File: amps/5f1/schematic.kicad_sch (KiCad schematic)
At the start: 26 parts, among them T2 8k:8

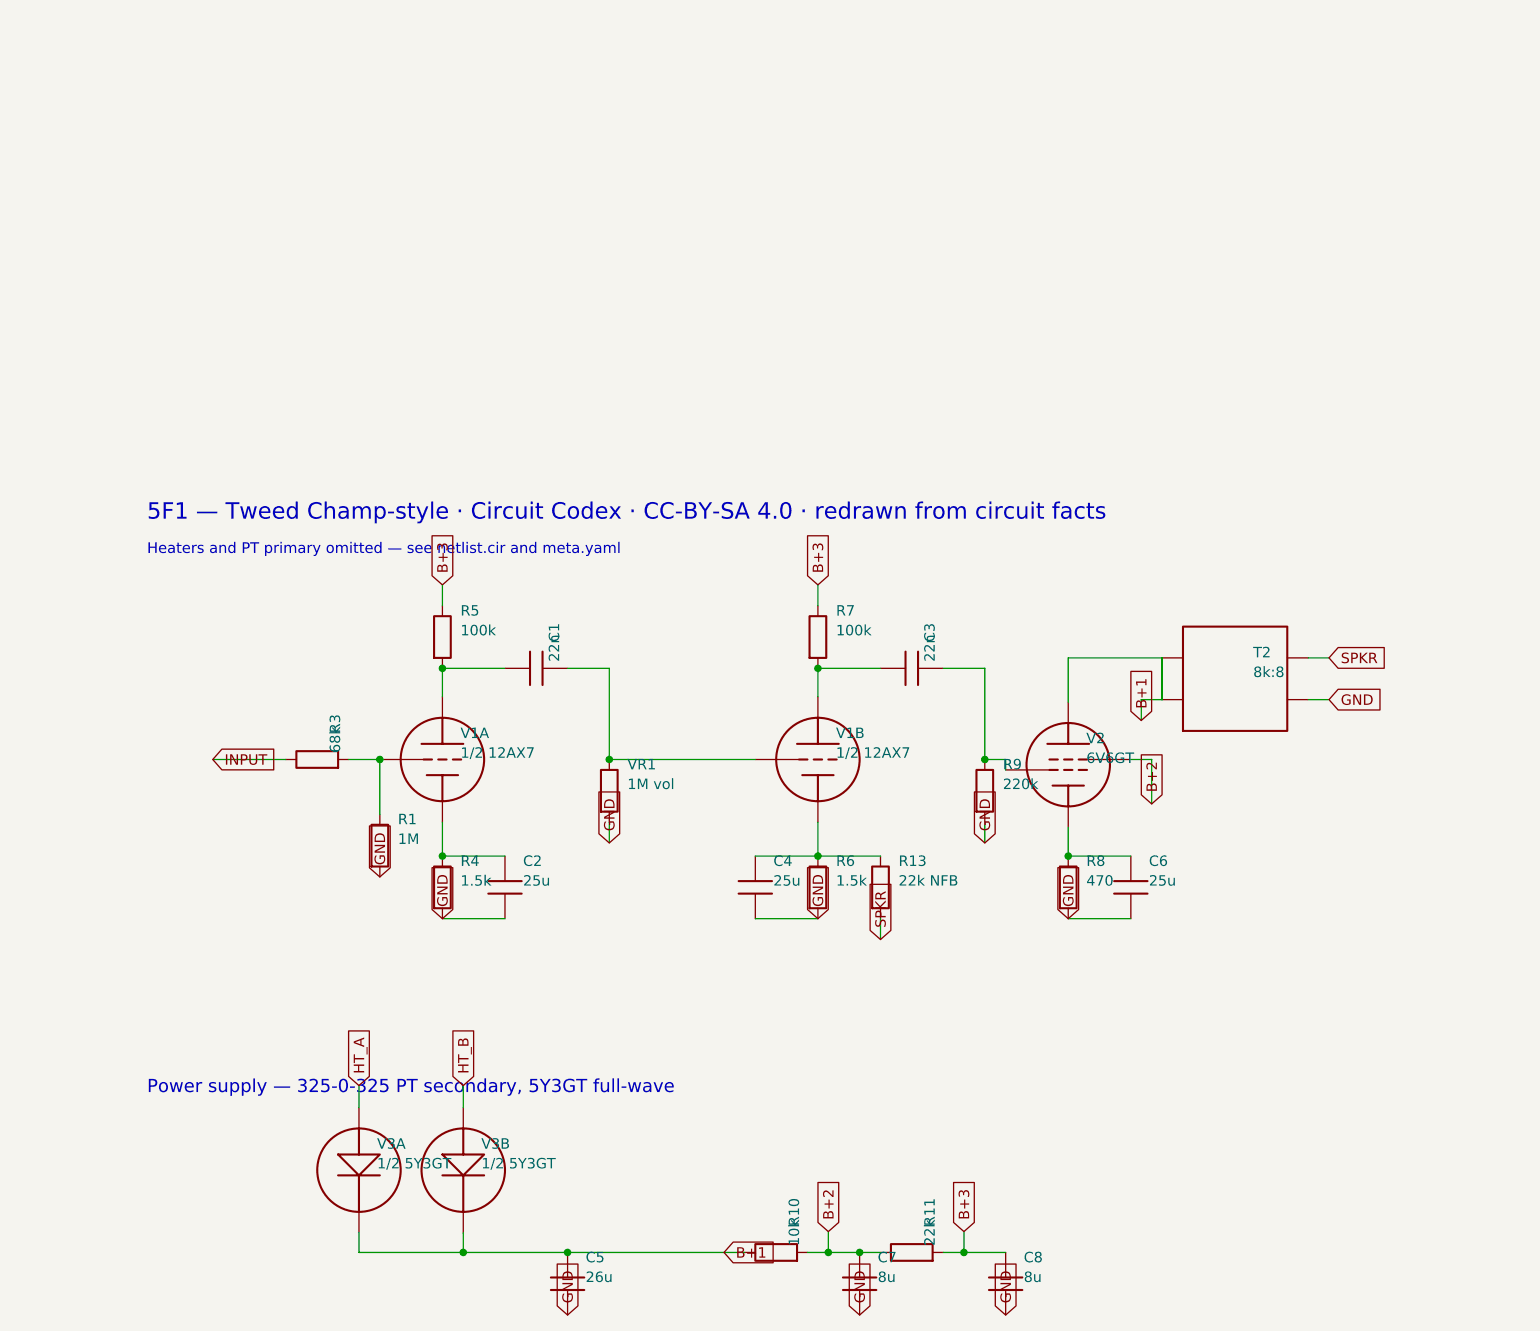
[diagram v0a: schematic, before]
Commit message: 5F1: ref-aligned parts list + schematic label readability pass
- amps/5f1/bom.yaml: every schematic reference designator (R1..R13,
  VR1, C1..C8, V1..V3, T2, PT) with part/value/rating/role — the
  substrate for Phase-1 vendor BOM links; rendered as a Parts list
  section on the amp page
- Schematic generator: property-angle compensation keeps labels
  horizontal on rotated symbols; labels repositioned clear of tube
  envelopes; rail-label stubs lifted off the resistor row; taller
  viewer (580px). Verified visually in Chrome.

Co-Authored-By: Claude Opus 4.8 (1M context) <noreply@anthropic.com>
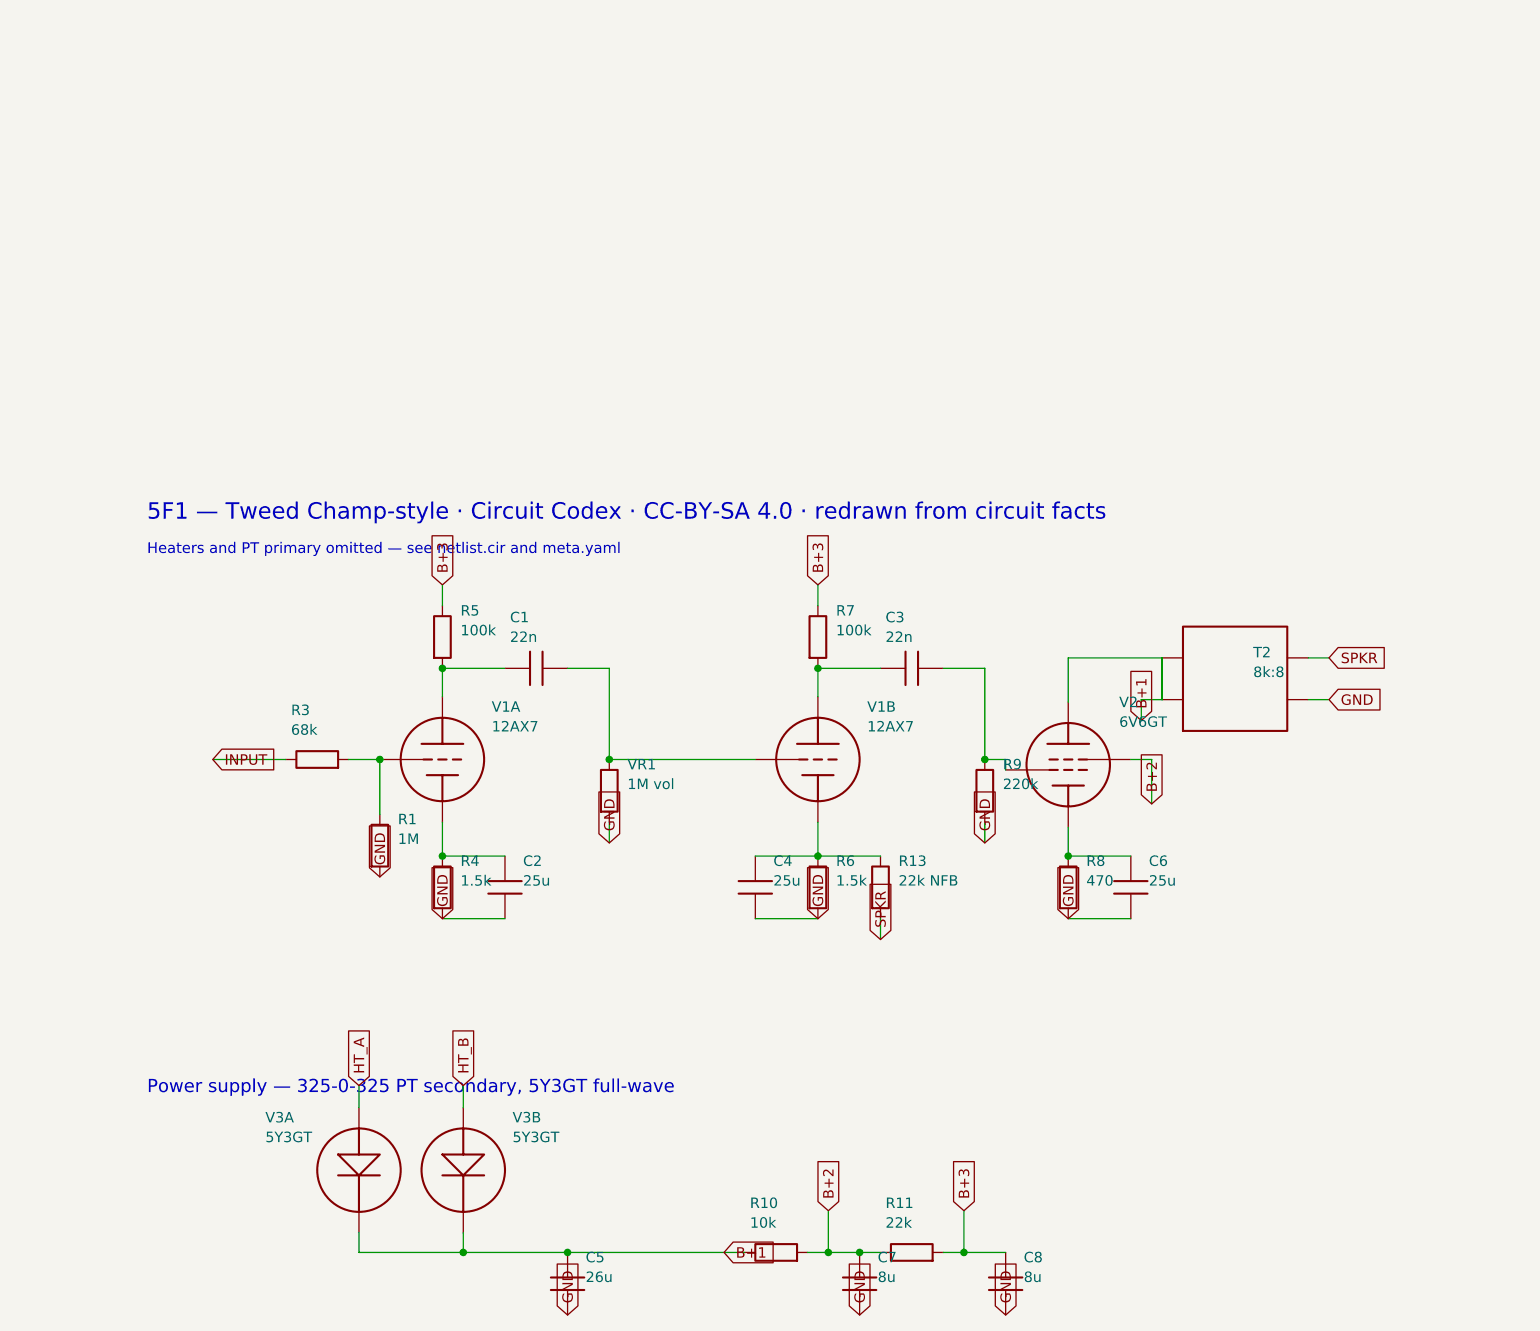
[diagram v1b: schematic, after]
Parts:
- V1A, V1B: value 1/2 12AX7 -> 12AX7
- V3A, V3B: value 1/2 5Y3GT -> 5Y3GT
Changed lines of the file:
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@@
   (symbol (lib_id "cx:R") (at 45.72 100 90) (unit 1)
     (in_bom yes) (on_board yes)
-    (property "Reference" "R3" (at 47.92 96.8 0) (effects (font (size 1.27 1.27)) (justify left)))
-    (property "Value" "68k" (at 47.92 99.2 0) (effects (font (size 1.27 1.27)) (justify left))))
+    (property "Reference" "R3" (at 42.52 94 270) (effects (font (size 1.27 1.27)) (justify left)))
+    (property "Value" "68k" (at 42.52 96.4 270) (effects (font (size 1.27 1.27)) (justify left))))
   (wire (pts (xy 49.53 100) (xy 53.34 100))
     (stroke (width 0) (type default)))
   (symbol (lib_id "cx:TRIODE") (at 60.96 100 0) (unit 1)
     (in_bom yes) (on_board yes)
-    (property "Reference" "V1A" (at 63.16 96.8 0) (effects (font (size 1.27 1.27)) (justify left)))
-    (property "Value" "1/2 12AX7" (at 63.16 99.2 0) (effects (font (size 1.27 1.27)) (justify left))))
+    (property "Reference" "V1A" (at 66.96 93.6 0) (effects (font (size 1.27 1.27)) (justify left)))
+    (property "Value" "12AX7" (at 66.96 96 0) (effects (font (size 1.27 1.27)) (justify left))))
   (junction (at 53.34 100) (diameter 0) (color 0 0 0 0))
   (symbol (lib_id "cx:R") (at 53.34 110.49 0) (unit 1)
@@
   (symbol (lib_id "cx:C") (at 72.39 88.9 90) (unit 1)
     (in_bom yes) (on_board yes)
-    (property "Reference" "C1" (at 74.59 85.7 0) (effects (font (size 1.27 1.27)) (justify left)))
-    (property "Value" "22n" (at 74.59 88.1 0) (effects (font (size 1.27 1.27)) (justify left))))
+    (property "Reference" "C1" (at 69.19 82.7 270) (effects (font (size 1.27 1.27)) (justify left)))
+    (property "Value" "22n" (at 69.19 85.1 270) (effects (font (size 1.27 1.27)) (justify left))))
   (wire (pts (xy 76.2 88.9) (xy 81.28 88.9))
     (stroke (width 0) (type default)))
@@
   (symbol (lib_id "cx:TRIODE") (at 106.68 100 0) (unit 1)
     (in_bom yes) (on_board yes)
-    (property "Reference" "V1B" (at 108.88 96.8 0) (effects (font (size 1.27 1.27)) (justify left)))
-    (property "Value" "1/2 12AX7" (at 108.88 99.2 0) (effects (font (size 1.27 1.27)) (justify left))))
+    (property "Reference" "V1B" (at 112.68 93.6 0) (effects (font (size 1.27 1.27)) (justify left)))
+    (property "Value" "12AX7" (at 112.68 96 0) (effects (font (size 1.27 1.27)) (justify left))))
   (wire (pts (xy 106.68 107.62) (xy 106.68 111.76))
     (stroke (width 0) (type default)))
@@
   (symbol (lib_id "cx:C") (at 118.11 88.9 90) (unit 1)
     (in_bom yes) (on_board yes)
-    (property "Reference" "C3" (at 120.31 85.7 0) (effects (font (size 1.27 1.27)) (justify left)))
-    (property "Value" "22n" (at 120.31 88.1 0) (effects (font (size 1.27 1.27)) (justify left))))
+    (property "Reference" "C3" (at 114.91 82.7 270) (effects (font (size 1.27 1.27)) (justify left)))
+    (property "Value" "22n" (at 114.91 85.1 270) (effects (font (size 1.27 1.27)) (justify left))))
   (wire (pts (xy 121.92 88.9) (xy 127 88.9))
     (stroke (width 0) (type default)))
@@
   (symbol (lib_id "cx:PENTODE") (at 137.16 100.635 0) (unit 1)
     (in_bom yes) (on_board yes)
-    (property "Reference" "V2" (at 139.36 97.435 0) (effects (font (size 1.27 1.27)) (justify left)))
-    (property "Value" "6V6GT" (at 139.36 99.835 0) (effects (font (size 1.27 1.27)) (justify left))))
+    (property "Reference" "V2" (at 143.36 93.035 0) (effects (font (size 1.27 1.27)) (justify left)))
+    (property "Value" "6V6GT" (at 143.36 95.435 0) (effects (font (size 1.27 1.27)) (justify left))))
   (wire (pts (xy 129.54 100) (xy 129.54 101.27))
     (stroke (width 0) (type default)))
@@
   (symbol (lib_id "cx:DIODE_TUBE") (at 50.8 150 0) (unit 1)
     (in_bom yes) (on_board yes)
-    (property "Reference" "V3A" (at 53 146.8 0) (effects (font (size 1.27 1.27)) (justify left)))
-    (property "Value" "1/2 5Y3GT" (at 53 149.2 0) (effects (font (size 1.27 1.27)) (justify left))))
+    (property "Reference" "V3A" (at 39.4 143.6 0) (effects (font (size 1.27 1.27)) (justify left)))
+    (property "Value" "5Y3GT" (at 39.4 146 0) (effects (font (size 1.27 1.27)) (justify left))))
   (global_label "HT_B" (shape input) (at 63.5 139.7 90)
     (effects (font (size 1.27 1.27)) (justify left)))
@@
   (symbol (lib_id "cx:DIODE_TUBE") (at 63.5 150 0) (unit 1)
     (in_bom yes) (on_board yes)
-    (property "Reference" "V3B" (at 65.7 146.8 0) (effects (font (size 1.27 1.27)) (justify left)))
-    (property "Value" "1/2 5Y3GT" (at 65.7 149.2 0) (effects (font (size 1.27 1.27)) (justify left))))
+    (property "Reference" "V3B" (at 69.5 143.6 0) (effects (font (size 1.27 1.27)) (justify left)))
+    (property "Value" "5Y3GT" (at 69.5 146 0) (effects (font (size 1.27 1.27)) (justify left))))
   (wire (pts (xy 50.8 157.62) (xy 50.8 160.02))
     (stroke (width 0) (type default)))
@@
   (symbol (lib_id "cx:R") (at 101.6 160.02 90) (unit 1)
     (in_bom yes) (on_board yes)
-    (property "Reference" "R10" (at 103.8 156.82 0) (effects (font (size 1.27 1.27)) (justify left)))
-    (property "Value" "10k" (at 103.8 159.22 0) (effects (font (size 1.27 1.27)) (justify left))))
+    (property "Reference" "R10" (at 98.4 154.02 270) (effects (font (size 1.27 1.27)) (justify left)))
+    (property "Value" "10k" (at 98.4 156.42 270) (effects (font (size 1.27 1.27)) (justify left))))
   (wire (pts (xy 105.41 160.02) (xy 114.3 160.02))
     (stroke (width 0) (type default)))
   (junction (at 107.95 160.02) (diameter 0) (color 0 0 0 0))
-  (global_label "B+2" (shape input) (at 107.95 157.48 90)
-    (effects (font (size 1.27 1.27)) (justify left)))
-  (wire (pts (xy 107.95 157.48) (xy 107.95 160.02))
+  (global_label "B+2" (shape input) (at 107.95 154.94 90)
+    (effects (font (size 1.27 1.27)) (justify left)))
+  (wire (pts (xy 107.95 154.94) (xy 107.95 160.02))
     (stroke (width 0) (type default)))
   (junction (at 111.76 160.02) (diameter 0) (color 0 0 0 0))
@@
   (symbol (lib_id "cx:R") (at 118.11 160.02 90) (unit 1)
     (in_bom yes) (on_board yes)
-    (property "Reference" "R11" (at 120.31 156.82 0) (effects (font (size 1.27 1.27)) (justify left)))
-    (property "Value" "22k" (at 120.31 159.22 0) (effects (font (size 1.27 1.27)) (justify left))))
+    (property "Reference" "R11" (at 114.91 154.02 270) (effects (font (size 1.27 1.27)) (justify left)))
+    (property "Value" "22k" (at 114.91 156.42 270) (effects (font (size 1.27 1.27)) (justify left))))
   (wire (pts (xy 121.92 160.02) (xy 129.54 160.02))
     (stroke (width 0) (type default)))
   (junction (at 124.46 160.02) (diameter 0) (color 0 0 0 0))
-  (global_label "B+3" (shape input) (at 124.46 157.48 90)
-    (effects (font (size 1.27 1.27)) (justify left)))
-  (wire (pts (xy 124.46 157.48) (xy 124.46 160.02))
+  (global_label "B+3" (shape input) (at 124.46 154.94 90)
+    (effects (font (size 1.27 1.27)) (justify left)))
+  (wire (pts (xy 124.46 154.94) (xy 124.46 160.02))
     (stroke (width 0) (type default)))
   (symbol (lib_id "cx:C") (at 129.54 163.83 0) (unit 1)

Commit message: Apply judge findings: 5F1 corrections from the K-EE drawing + site polish
The editorial/accuracy judge's first run (12 findings) applied:
- 5F1 re-verified against the published K-EE schematic directly:
  filter caps are 16/8/8 uF (the 26 uF chart read-off was a misread
  16), couplers .02-600, droppers 10k+22k now confirmed in print,
  OT unmarked -> listed as ~5k:8 typical SE 6V6 load (was 8k:8);
  wattage aligned to 5 W everywhere
- 5F1 notes: single consistent chart table (dropper discrimination
  reduced to the rail rows), remaining working-notes voice removed
- Tolerance column explained site-wide (project targets vs Fender's
  printed +/-20% convention); unit house style in tables and prose;
  thin table notes filled

Co-Authored-By: Claude Opus 4.8 (1M context) <noreply@anthropic.com>
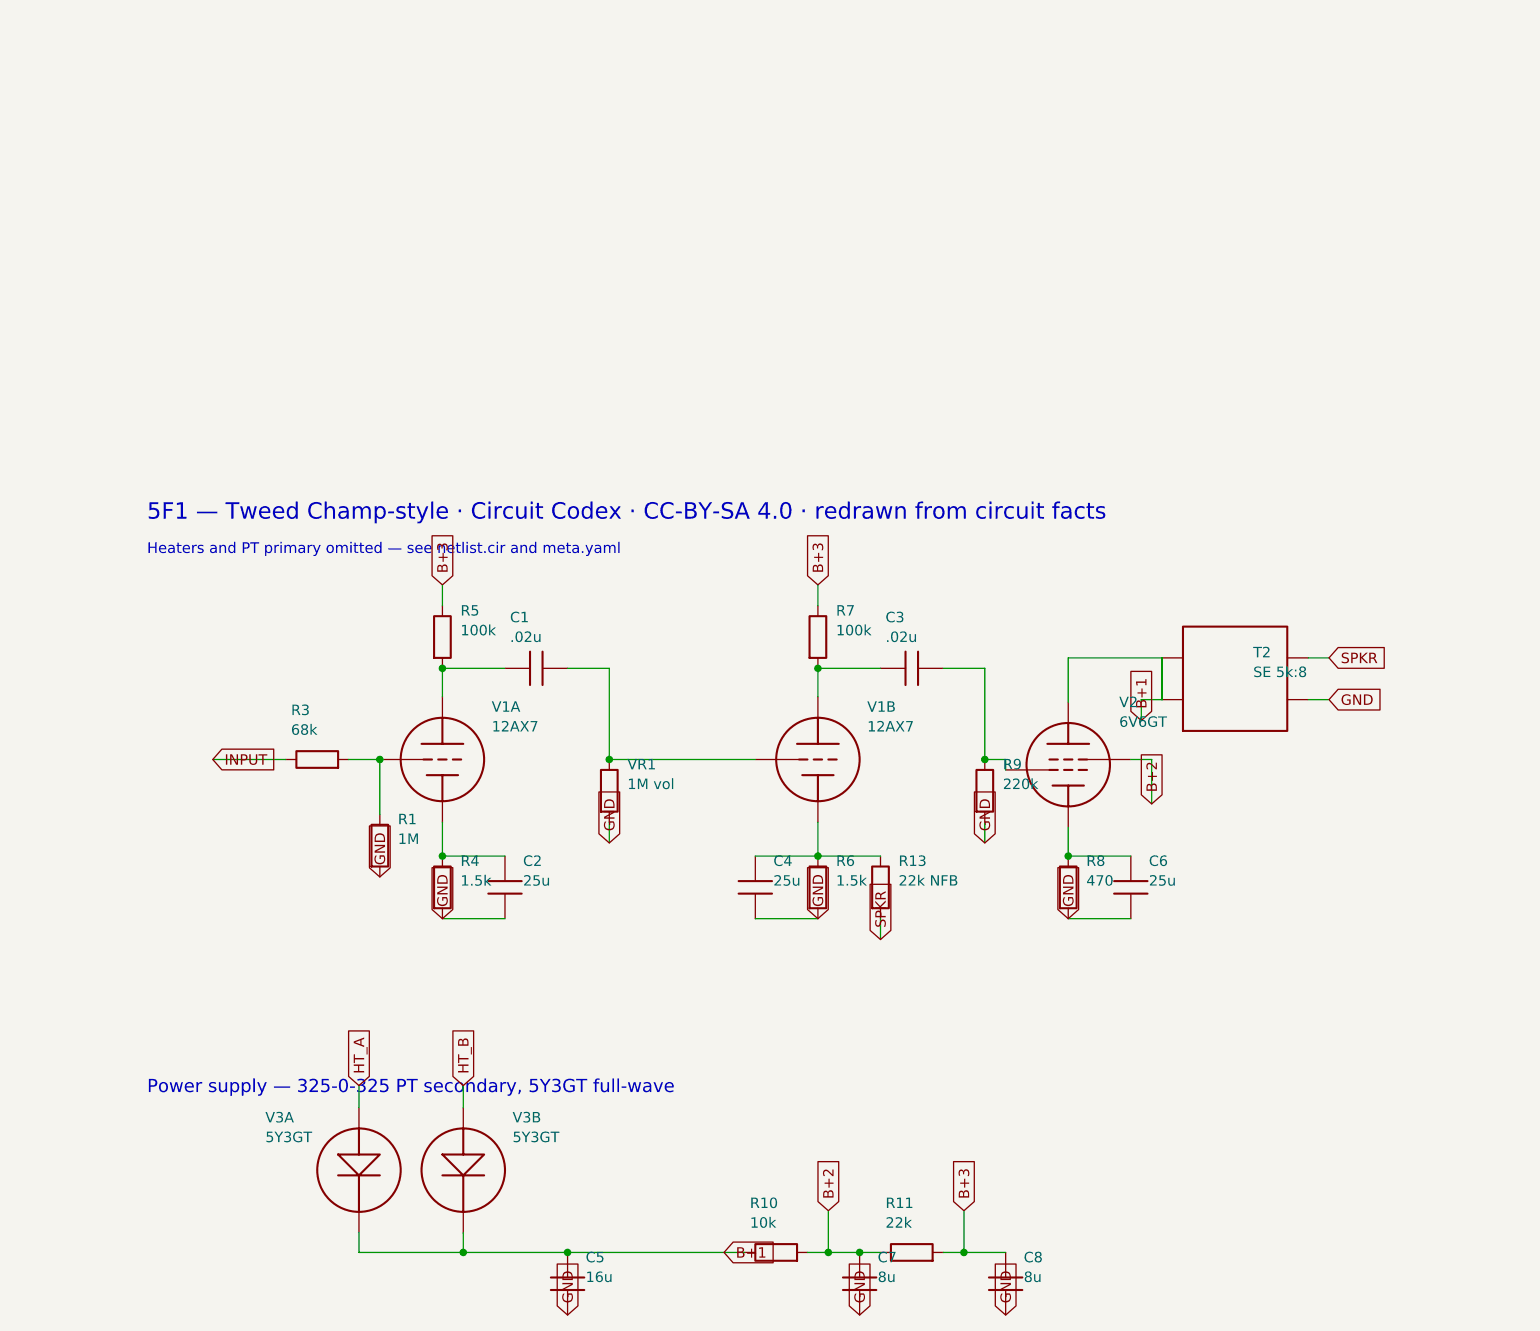
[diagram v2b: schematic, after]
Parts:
- C1, C3: value 22n -> .02u
- C5: value 26u -> 16u
- T2: value 8k:8 -> SE 5k:8
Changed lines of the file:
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@@
     (in_bom yes) (on_board yes)
     (property "Reference" "C1" (at 69.19 82.7 270) (effects (font (size 1.27 1.27)) (justify left)))
-    (property "Value" "22n" (at 69.19 85.1 270) (effects (font (size 1.27 1.27)) (justify left))))
+    (property "Value" ".02u" (at 69.19 85.1 270) (effects (font (size 1.27 1.27)) (justify left))))
   (wire (pts (xy 76.2 88.9) (xy 81.28 88.9))
     (stroke (width 0) (type default)))
@@
     (in_bom yes) (on_board yes)
     (property "Reference" "C3" (at 114.91 82.7 270) (effects (font (size 1.27 1.27)) (justify left)))
-    (property "Value" "22n" (at 114.91 85.1 270) (effects (font (size 1.27 1.27)) (justify left))))
+    (property "Value" ".02u" (at 114.91 85.1 270) (effects (font (size 1.27 1.27)) (justify left))))
   (wire (pts (xy 121.92 88.9) (xy 127 88.9))
     (stroke (width 0) (type default)))
@@
     (in_bom yes) (on_board yes)
     (property "Reference" "T2" (at 159.68 86.97 0) (effects (font (size 1.27 1.27)) (justify left)))
-    (property "Value" "8k:8" (at 159.68 89.37 0) (effects (font (size 1.27 1.27)) (justify left))))
+    (property "Value" "SE 5k:8" (at 159.68 89.37 0) (effects (font (size 1.27 1.27)) (justify left))))
   (wire (pts (xy 148.59 87.63) (xy 148.59 87.63))
     (stroke (width 0) (type default)))
@@
     (in_bom yes) (on_board yes)
     (property "Reference" "C5" (at 78.4 160.63 0) (effects (font (size 1.27 1.27)) (justify left)))
-    (property "Value" "26u" (at 78.4 163.03 0) (effects (font (size 1.27 1.27)) (justify left))))
+    (property "Value" "16u" (at 78.4 163.03 0) (effects (font (size 1.27 1.27)) (justify left))))
   (global_label "GND" (shape input) (at 76.2 167.64 270)
     (effects (font (size 1.27 1.27)) (justify left)))
